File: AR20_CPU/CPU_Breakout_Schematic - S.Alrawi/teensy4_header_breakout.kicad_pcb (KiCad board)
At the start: 4 copper layers, 11 parts, among them J1 Conn_2Rows-34Pins, J3 Micro_SD_Card, SW1 SW_SPST, U1 Teensy_pins, U2 MCP2551-I-SN

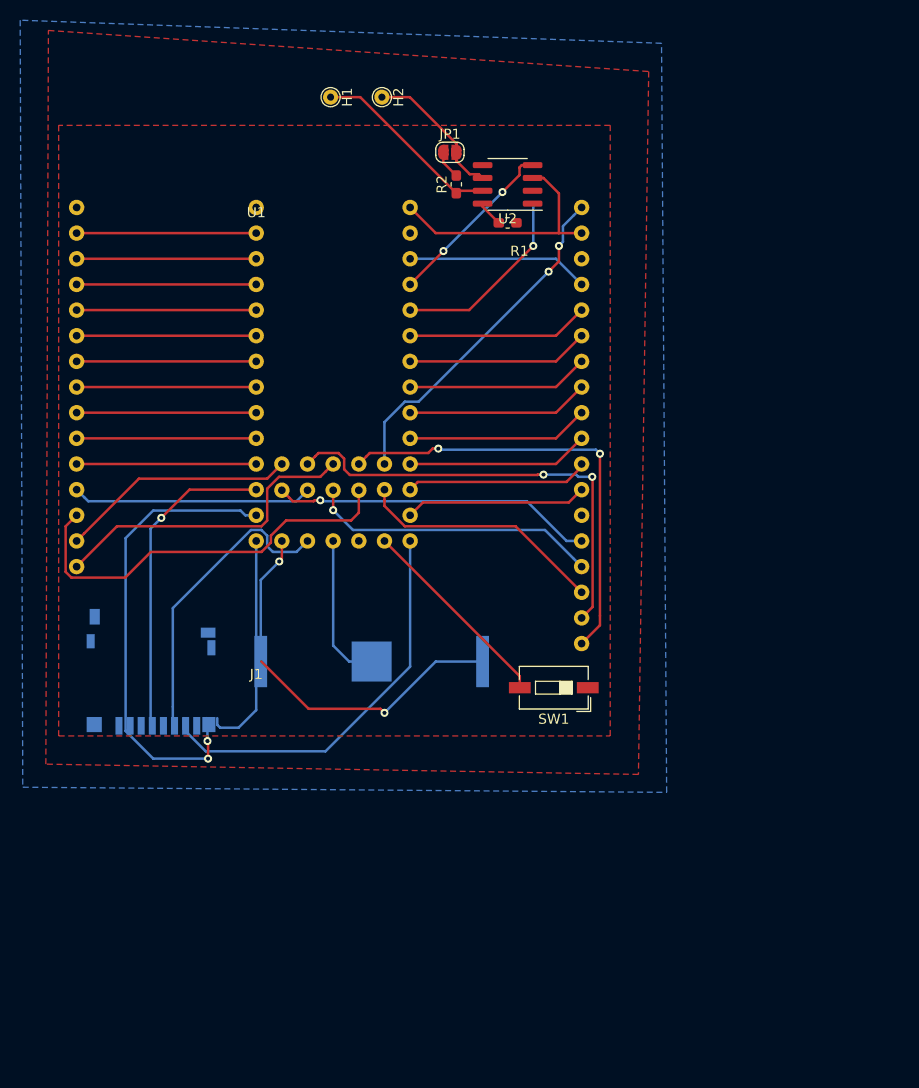
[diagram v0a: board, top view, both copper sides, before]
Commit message: Edited library
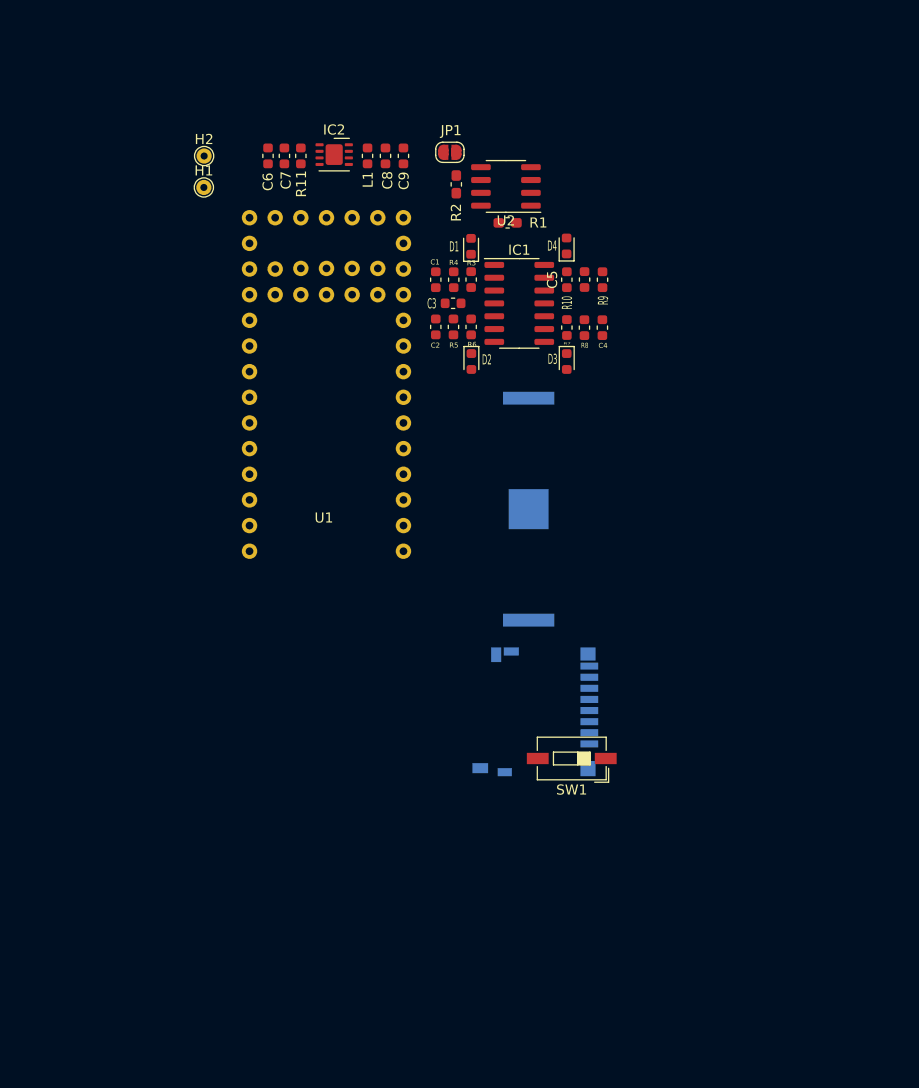
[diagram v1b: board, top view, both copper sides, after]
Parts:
- removed J1: Conn_2Rows-34Pins, Teensy_Footprint_Library:PINS_IO_TEENSY
- added C1: 1.5n, Capacitor_SMD:C_0603_1608Metric, F.Cu at (142.7, 79.3)
- added C2: 1.5n, Capacitor_SMD:C_0603_1608Metric, F.Cu at (142.7, 84.0)
- added C3: C, Capacitor_SMD:C_0603_1608Metric, F.Cu at (144.5, 81.6)
- added C4: 1.5n, Capacitor_SMD:C_0603_1608Metric, F.Cu at (159.2, 84.0)
- added C5: 1.5n, Capacitor_SMD:C_0603_1608Metric, F.Cu at (155.7, 79.3)
- added C6: 10u, Capacitor_SMD:C_0603_1608Metric, F.Cu at (126.1, 67.0)
- added C7: 0.1u, Capacitor_SMD:C_0603_1608Metric, F.Cu at (127.8, 67.0)
- added C8: 0.1u, Capacitor_SMD:C_0603_1608Metric, F.Cu at (137.8, 67.0)
- added C9: 10u, Capacitor_SMD:C_0603_1608Metric, F.Cu at (139.5, 67.0)
- added D1: 3V, Diode_SMD:D_0603_1608Metric, F.Cu at (146.2, 76.0)
- added D2: 3V, Diode_SMD:D_0603_1608Metric, F.Cu at (146.3, 87.4)
- added D3: 3V, Diode_SMD:D_0603_1608Metric, F.Cu at (155.7, 87.4)
- added D4: 3V, Diode_SMD:D_0603_1608Metric, F.Cu at (155.7, 75.9)
- added IC1: LM324DRG3, Package_SO:SOIC-14_3.9x8.7mm_P1.27mm, F.Cu at (151.0, 81.6)
- added IC2: NCV890430MW50TXG, Package_DFN_QFN:DFN-8-1EP_3x3mm_P0.65mm_EP1.7x2.05mm, F.Cu at (132.7, 66.9)
- added L1: 2.2u, Inductor_SMD:L_0603_1608Metric, F.Cu at (136.0, 67.0)
- added R10: 20k, Resistor_SMD:R_0603_1608Metric, F.Cu at (157.5, 79.3)
- added R11: 10k, Resistor_SMD:R_0603_1608Metric, F.Cu at (129.4, 67.0)
- added R3: 10k, Resistor_SMD:R_0603_1608Metric, F.Cu at (146.2, 79.3)
- added R4: 20k, Resistor_SMD:R_0603_1608Metric, F.Cu at (144.5, 79.3)
- added R5: 10k, Resistor_SMD:R_0603_1608Metric, F.Cu at (146.2, 84.0)
- added R6: 20k, Resistor_SMD:R_0603_1608Metric, F.Cu at (144.5, 84.0)
- added R7: 10k, Resistor_SMD:R_0603_1608Metric, F.Cu at (155.7, 84.0)
- added R8: 20k, Resistor_SMD:R_0603_1608Metric, F.Cu at (157.5, 84.0)
- added R9: 10k, Resistor_SMD:R_0603_1608Metric, F.Cu at (159.3, 79.3)
- moved J3 38.3 mm to (152.6, 122.1), turned to 270 degrees
- moved U1 37.0 mm to (139.5, 106.2), turned to 180 degrees
- moved BT1 21.7 mm to (151.9, 102.0), turned to 270 degrees
- moved H2 18.5 mm to (119.8, 67.0), turned to 0 degrees
- moved H1 15.4 mm to (119.8, 70.2), turned to 0 degrees
- moved SW1 7.23 mm to (156.2, 126.7)
- moved U2 0.26 mm to (149.7, 70.1)
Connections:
- J3 pad 2: 10_CS -> (no net)
- J3 pad 3: (no net) -> 10_CS
- U1 pad 12: 21_A7 -> Out1
- U1 pad 14: 20_A6 -> Out2
- U1 pad 16: 19_A5 -> Out3
- U1 pad 18: 18_A4 -> Out4
- U1 pad 32: PROGRAMM -> (no net)
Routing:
- net 11_MOSI: track 46.7 -> 0.00 mm, vias 2 -> 0
- net 30_CRX3: track 44.7 -> 0.00 mm, vias 2 -> 0
- net 32_OUT1B: track 44.3 -> 0.00 mm, vias 2 -> 0
- net 27_A13: track 40.6 -> 0.00 mm
- net 13(LED): track 40.3 -> 0.00 mm
- net VBAT: track 38.9 -> 0.00 mm, vias 2 -> 0
- net 33_MCLK2: track 34.3 -> 0.00 mm, vias 2 -> 0
- net 24_A10: track 31.8 -> 0.00 mm, vias 1 -> 0
- net 31_CTX3: track 31.5 -> 0.00 mm
- net 10_CS: track 30.8 -> 0.00 mm, vias 1 -> 0
- net 3V3: track 29.4 -> 0.00 mm
- net 26_A12: track 28.9 -> 0.00 mm, vias 1 -> 0
- net Vinn_5V: track 25.2 -> 0.00 mm
- net 28_RX7: track 24.7 -> 0.00 mm
- net 25_A11: track 23.8 -> 0.00 mm
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- removed copper zone on B.Cu, net Ground
- removed copper zone on F.Cu, net Ground
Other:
- copper layers 4 -> 2
- rule pad_to_mask_clearance: 0 -> 0.0508
- rule trace_min: 0.007 -> 0.25

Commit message: Edited the layout
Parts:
- removed J3: Micro_SD_Card, Connector_Card:microSD_HC_Hirose_DM3D-SF
- removed U1: Teensy_pins, Teensy_Footprint_Library:Teensy_40_footprint
- removed U2: MCP2551-I-SN, Package_SO:SOIC-8_3.9x4.9mm_P1.27mm
- added C10: 1.5n, Capacitor_SMD:C_0603_1608Metric, F.Cu at (158.2, 81.4)
- added CANmodule1: MCP2551-I-SN, Package_SO:SOIC-8_3.9x4.9mm_P1.27mm, F.Cu at (138.5, 82.9)
- added GND1: GND, TestPoint:TestPoint_THTPad_D1.5mm_Drill0.7mm, F.Cu at (116.7, 117.3)
- added J1: MX34_36_pins, Teensy_Footprint_Library:Connector_MX34_36pins, F.Cu at (131.2, 124.8)
- added JP2: SJ_Open, Jumper:SolderJumper-2_P1.3mm_Open_RoundedPad1.0x1.5mm, B.Cu at (143.3, 80.0)
- added JP3: SJ_Open, Jumper:SolderJumper-2_P1.3mm_Open_RoundedPad1.0x1.5mm, B.Cu at (143.5, 86.2)
- added JP4: SJ_Open, Jumper:SolderJumper-2_P1.3mm_Open_RoundedPad1.0x1.5mm, F.Cu at (159.2, 89.0)
- added JP5: SJ_Open, Jumper:SolderJumper-2_P1.3mm_Open_RoundedPad1.0x1.5mm, F.Cu at (158.5, 78.2)
- added MX34_Housing1: MX34_Housing, Teensy_Footprint_Library:Housing_3pins, F.Cu at (116.7, 130.6)
- added R12: 20k, Resistor_SMD:R_0603_1608Metric, F.Cu at (156.3, 81.4)
- added SDcard1: Micro_SD_Card, Connector_Card:microSD_HC_Hirose_DM3D-SF, F.Cu at (119.8, 83.0)
- added Teensy4.0: Teensy_pins, Teensy_Footprint_Library:Teensy_40_footprint, F.Cu at (123.3, 107.7)
- C2: value 1.5n -> 10u
- R6: value 20k -> 10k
- moved SW1 47.7 mm to (116.1, 101.0), turned to 270 degrees
- moved H2 45.3 mm to (116.7, 112.2)
- moved H1 44.7 mm to (116.8, 114.8)
- moved R6 27.7 mm to (117.7, 90.7), turned to 180 degrees
- moved C9 24.0 mm to (130.7, 89.3), turned to 0 degrees
- moved BT1 22.0 mm to (141.4, 121.3), turned to 180 degrees
- moved C8 21.7 mm to (130.7, 87.5), turned to 0 degrees
- moved L1 19.4 mm to (130.7, 85.7), turned to 180 degrees
- moved R1 16.6 mm to (134.8, 80.8), turned to 90 degrees
- moved C4 15.9 mm to (143.5, 86.1)
- moved SWReg_NVC1 15.6 mm to (130.8, 82.4), turned to 270 degrees
- moved R8 12.5 mm to (145.2, 86.1)
- moved R11 12.2 mm to (130.7, 79.1), turned to 180 degrees
- moved JP1 10.9 mm to (141.9, 77.3), turned to 270 degrees
- moved C7 10.9 mm to (130.7, 77.5), turned to 180 degrees
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- renumbered IC1 to LM324, IC2 to SWReg_NVC1
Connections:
- BT1 pad 2: GND_BATT -> Ground
- C1 pad 2: Ground -> Net-(C1-Pad2)
- C2 pad 1: IN2+ -> Vinn_5V
- C2 pad 2: Ground -> Net-(C2-Pad2)
- C4 pad 1: IN3+ -> IN2+
- C4 pad 2: Ground -> Net-(C4-Pad2)
- C5 pad 1: IN4+ -> IN3+
- C5 pad 2: Ground -> Net-(C5-Pad2)
- LM324 pad 11: (no net) -> Ground
- R10 pad 1: IN4+ -> IN3+
- R3 pad 1: (no net) -> Sensor_Input_1
- R5 pad 1: (no net) -> Sensor_Input_2
- R6 pad 1: IN2+ -> 3.3V
- R6 pad 2: Ground -> 13(LED)
- R7 pad 1: (no net) -> Sensor_Input_3
- R8 pad 1: IN3+ -> IN2+
- R9 pad 1: (no net) -> Sensor_Input_4
- SWReg_NVC1 pad 9: Ground -> (no net)
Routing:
- net 12V_IN: track 0.00 -> 78.1 mm, vias 0 -> 4
- net 13(LED): track 0.00 -> 66.4 mm, vias 0 -> 2
- net 11_MOSI: track 0.00 -> 62.9 mm, vias 0 -> 4
- net Net-(CANmodule1-Pad6): track 0.00 -> 62.5 mm, vias 0 -> 3
- net 12_MISO: track 0.00 -> 58.5 mm, vias 0 -> 5
- net 10_CS: track 0.00 -> 57.5 mm, vias 0 -> 1
- net Net-(CANmodule1-Pad7): track 0.00 -> 55.0 mm, vias 0 -> 3
- net ON_OFF: track 0.00 -> 52.0 mm, vias 0 -> 1
- net Vinn_5V: track 0.00 -> 50.3 mm, vias 0 -> 4
- net VBAT: track 0.00 -> 45.8 mm
- net Sensor_Input_1: track 0.00 -> 39.6 mm, vias 0 -> 2
- net 15_A1: track 0.00 -> 38.3 mm
- net 16_A2: track 0.00 -> 38.1 mm
- net 17_A3: track 0.00 -> 37.9 mm
- net Sensor_Input_4: track 0.00 -> 36.7 mm
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- added copper zone on B.Cu, net Ground
- added copper zone on F.Cu, net Ground
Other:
- board outline added: 57 x 60 mm
- board text added: "AR20 Teensy 4.0"

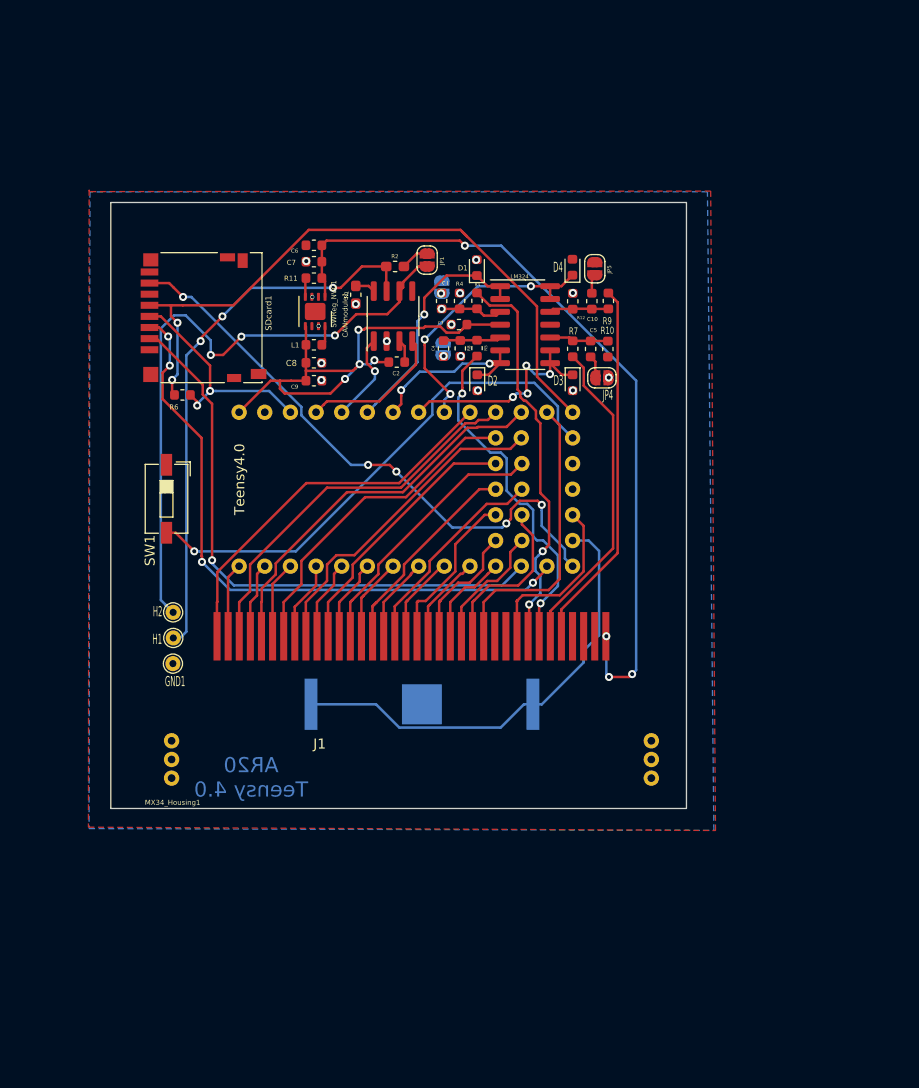
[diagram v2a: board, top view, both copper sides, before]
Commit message: Edited to 4 layers
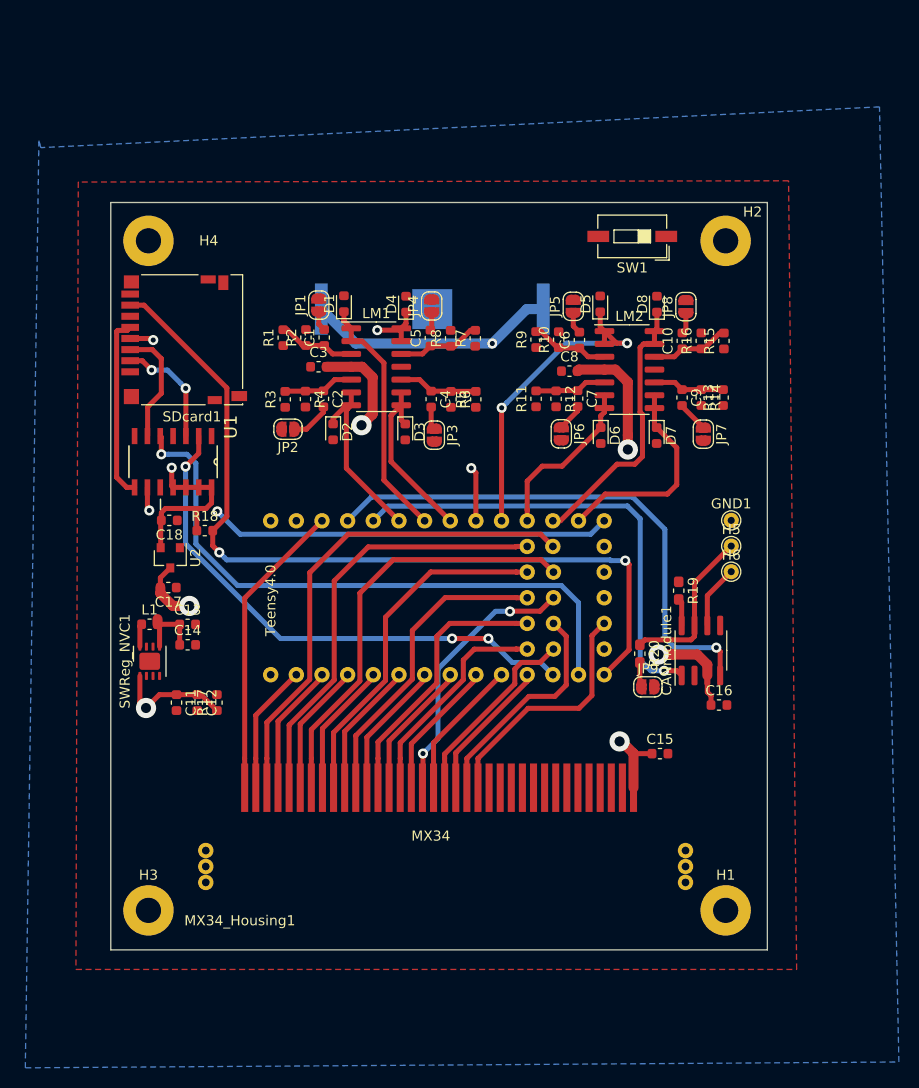
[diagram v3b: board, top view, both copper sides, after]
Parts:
- removed J1: MX34_36_pins, Teensy_Footprint_Library:Connector_MX34_36pins
- removed LM324: LM324DRG3, Package_SO:SOIC-14_3.9x8.7mm_P1.27mm
- added C11: 10u, Capacitor_SMD:C_0603_1608Metric, F.Cu at (117.1, 121.2)
- added C12: 0.1u, Capacitor_SMD:C_0603_1608Metric, F.Cu at (119.1, 121.2)
- added C13: 0.1u, Capacitor_SMD:C_0603_1608Metric, F.Cu at (118.2, 113.4)
- added C14: 10u, Capacitor_SMD:C_0603_1608Metric, F.Cu at (118.2, 115.4)
- added C15: 10u, Capacitor_SMD:C_0603_1608Metric, F.Cu at (164.9, 126.2)
- added C16: 100u, Capacitor_SMD:C_0603_1608Metric, F.Cu at (170.8, 121.4)
- added C17: 100u, Capacitor_SMD:C_0603_1608Metric, F.Cu at (116.3, 109.8)
- added C18: 100u, Capacitor_SMD:C_0603_1608Metric, F.Cu at (116.4, 103.1)
- added D5: 3V, Diode_SMD:D_0603_1608Metric, F.Cu at (159.0, 81.7)
- added D6: 3V, Diode_SMD:D_0603_1608Metric, F.Cu at (159.1, 94.7)
- added D7: 3V, Diode_SMD:D_0603_1608Metric, F.Cu at (164.6, 94.7)
- added D8: 3V, Diode_SMD:D_0603_1608Metric, F.Cu at (164.6, 81.7)
- added H3: MountingHole, MountingHole:MountingHole_2.5mm_Pad, F.Cu at (114.3, 141.7)
- added H4: MountingHole, MountingHole:MountingHole_2.5mm_Pad, F.Cu at (114.3, 75.4)
- added H5: CANH_out, TestPoint:TestPoint_THTPad_D1.5mm_Drill0.7mm, F.Cu at (172.0, 105.7)
- added H6: CANL_out, TestPoint:TestPoint_THTPad_D1.5mm_Drill0.7mm, F.Cu at (172.0, 108.2)
- added JP6: SJ_Open, Jumper:SolderJumper-2_P1.3mm_Open_RoundedPad1.0x1.5mm, F.Cu at (155.2, 94.5)
- added JP7: SJ_Open, Jumper:SolderJumper-2_P1.3mm_Open_RoundedPad1.0x1.5mm, F.Cu at (169.2, 94.6)
- added JP8: SJ_Open, Jumper:SolderJumper-2_P1.3mm_Open_RoundedPad1.0x1.5mm, F.Cu at (167.5, 82.0)
- added JP9: SolderJumper_2_Open, Jumper:SolderJumper-2_P1.3mm_Open_RoundedPad1.0x1.5mm, F.Cu at (163.8, 119.6)
- added LM1: LM324DRG3, Package_SO:SOIC-14_3.9x8.7mm_P1.27mm, F.Cu at (136.9, 87.9)
- added LM2: LM324DRG3, Package_SO:SOIC-14_3.9x8.7mm_P1.27mm, F.Cu at (161.9, 88.2)
- added MX34: MX34_36_pins, Teensy_Footprint_Library:Connector_MX34_36pins, F.Cu at (134.0, 139.7)
- added R13: 10k, Resistor_SMD:R_0603_1608Metric, F.Cu at (171.2, 91.0)
- added R14: 20k, Resistor_SMD:R_0603_1608Metric, F.Cu at (169.0, 91.0)
- added R15: 10k, Resistor_SMD:R_0603_1608Metric, F.Cu at (171.3, 85.4)
- added R16: 20k, Resistor_SMD:R_0603_1608Metric, F.Cu at (169.0, 85.3)
- added R17: 10k, Resistor_SMD:R_0603_1608Metric, F.Cu at (121.1, 121.2)
- added R18: 10k, Resistor_SMD:R_0603_1608Metric, F.Cu at (119.9, 104.1)
- added R19: 60, Resistor_SMD:R_0603_1608Metric_Pad1.05x0.95mm_HandSolder, F.Cu at (166.8, 110.1)
- added R20: 120, Resistor_SMD:R_0603_1608Metric_Pad1.05x0.95mm_HandSolder, F.Cu at (163.0, 116.3)
- added U1: 74LCX125M, SamacSys_Parts:SOIC127P600X175-14N, F.Cu at (116.7, 97.3)
- added U2: MCP1700_SOT23, Package_TO_SOT_SMD:SOT-23, F.Cu at (116.5, 106.8)
- C2, C6, C9: value 10u -> 1.5n
- C7: value 0.1u -> 1.5n
- C8: value 0.1u -> C
- H1: value CANH_out -> GND; footprint TestPoint:TestPoint_THTPad_D1.5mm_Drill0.7mm -> MountingHole:MountingHole_2.5mm_Pad
- H2: value CANL_out -> MountingHole; footprint TestPoint:TestPoint_THTPad_D1.5mm_Drill0.7mm -> MountingHole:MountingHole_2.5mm_Pad
- JP1: value SolderJumper_2_Open -> SJ_Open
- JP2, JP3: moved to F.Cu
- R1: value 60 -> 10k; footprint Resistor_SMD:R_0603_1608Metric_Pad1.05x0.95mm_HandSolder -> Resistor_SMD:R_0603_1608Metric
- R2: value 120 -> 20k; footprint Resistor_SMD:R_0603_1608Metric_Pad1.05x0.95mm_HandSolder -> Resistor_SMD:R_0603_1608Metric
- R6: value 10k -> 20k
- moved H2 65.9 mm to (171.4, 75.4)
- moved H1 61.0 mm to (171.4, 141.7)
- moved GND1 57.1 mm to (172.0, 103.1)
- moved SW1 52.9 mm to (162.2, 75.0), turned to 180 degrees
- moved CANmodule1 45.0 mm to (169.0, 116.0)
- moved BT1 39.1 mm to (142.4, 82.2), turned to 0 degrees
- moved SWReg_NVC1 38.3 mm to (114.4, 117.1), turned to 90 degrees
- moved C9 36.5 mm to (167.1, 91.0), turned to 270 degrees
- moved L1 32.1 mm to (114.4, 113.4), turned to 0 degrees
- moved C7 29.4 mm to (156.8, 91.1), turned to 270 degrees
- moved C6 27.9 mm to (157.0, 85.3), turned to 90 degrees
- moved R6 26.6 mm to (144.2, 91.1), turned to 270 degrees
- moved C8 25.3 mm to (156.0, 88.3)
- moved R11 25.0 mm to (152.7, 91.1), turned to 90 degrees
- moved R3 21.3 mm to (127.8, 91.1), turned to 90 degrees
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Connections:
- C10 pad 1: IN4+ -> IN8+
- C2 pad 1: Vinn_5V -> IN2+
- C4 pad 1: IN2+ -> IN3+
- C5 pad 1: IN3+ -> IN4+
- C6 pad 1: 12V_IN -> IN5+
- C6 pad 2: Ground -> Net-(C6-Pad2)
- C7 pad 1: 12V_IN -> IN6+
- C7 pad 2: Ground -> Net-(C7-Pad2)
- C8 pad 1: Vinn_5V -> Ground
- C8 pad 2: Ground -> Vinn_5V
- C9 pad 1: Vinn_5V -> IN7+
- C9 pad 2: Ground -> Net-(C9-Pad2)
- CANmodule1 pad 3: Net-(C2-Pad2) -> Vinn_5V
- H1 pad 1: Net-(CANmodule1-Pad7) -> (no net)
- H2 pad 1: Net-(CANmodule1-Pad6) -> (no net)
- JP1 pad 1: Net-(JP1-Pad1) -> Net-(C1-Pad2)
- JP1 pad 2: Net-(CANmodule1-Pad6) -> Ground
- JP2 pad 1: Net-(C1-Pad2) -> Net-(C2-Pad2)
- JP5 pad 1: Net-(C10-Pad2) -> Net-(C6-Pad2)
- R1 pad 1: Ground -> Sensor_Input_1
- R1 pad 2: Net-(CANmodule1-Pad8) -> IN1+
- R10 pad 1: IN3+ -> IN5+
- R11 pad 1: 12V_IN -> Sensor_Input_6
- R11 pad 2: Net-(R11-Pad2) -> IN6+
- R12 pad 1: IN4+ -> IN6+
- R2 pad 1: Net-(CANmodule1-Pad7) -> IN1+
- R2 pad 2: Net-(JP1-Pad1) -> Ground
- R3 pad 1: Sensor_Input_1 -> Sensor_Input_2
- R3 pad 2: IN1+ -> IN2+
- R4 pad 1: IN1+ -> IN2+
- R5 pad 1: Sensor_Input_2 -> Sensor_Input_3
- R5 pad 2: IN2+ -> IN3+
- R6 pad 1: 3.3V -> IN3+
- R6 pad 2: 13(LED) -> Ground
- R7 pad 1: Sensor_Input_3 -> Sensor_Input_4
- R7 pad 2: IN3+ -> IN4+
- R8 pad 1: IN2+ -> IN4+
- R9 pad 1: Sensor_Input_4 -> Sensor_Input_5
- R9 pad 2: IN4+ -> IN5+
- SDcard1 pad 2: 10_CS -> CS_3.3V
- SDcard1 pad 3: 11_MOSI -> MOSI_3.3V
- SDcard1 pad 4: 3.3V -> 3V3_SD
- SDcard1 pad 5: 13(LED) -> SCLK_3.3V
- SWReg_NVC1 pad 4: Net-(R11-Pad2) -> Net-(R17-Pad2)
- SWReg_NVC1 pad 9: (no net) -> Ground
- Teensy4.0 pad 12: Out1 -> Out2
- Teensy4.0 pad 14: Out2 -> Out1
- Teensy4.0 pad 20: 17_A3 -> Out5
- Teensy4.0 pad 22: 16_A2 -> Out6
- Teensy4.0 pad 24: 15_A1 -> Out8
- Teensy4.0 pad 26: 14_A0 -> Out7
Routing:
- net Vinn_5V: track 50.3 -> 145.5 mm
- net Net-(CANmodule1-Pad6): track 62.5 -> 6.30 mm, vias 3 -> 0
- net ON_OFF: track 52.0 -> 0.00 mm, vias 1 -> 0
- net Sensor_Input_1: track 39.6 -> 0.00 mm, vias 2 -> 0
- net Net-(CANmodule1-Pad7): track 55.0 -> 16.2 mm, vias 3 -> 0
- net 23_CRX1: track 14.3 -> 52.9 mm, vias 0 -> 1
- net 15_A1: track 38.3 -> 0.00 mm
- net 16_A2: track 38.1 -> 0.00 mm
- net 17_A3: track 37.9 -> 0.00 mm
- net 22_CTX1: track 9.02 -> 46.3 mm
- net Sensor_Input_4: track 36.7 -> 0.00 mm
- net Sensor_Input_2: track 34.7 -> 0.00 mm, vias 2 -> 0
- net 3V3_SD: track 0.00 -> 34.2 mm, vias 0 -> 2
- net Out5: track 0.00 -> 32.4 mm, vias 0 -> 2
- net Sensor_Input_3: track 31.9 -> 0.00 mm
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- added copper zone on Back_2_3V3, net 3V3_SD
- added copper zone on Front_2_5V, net Vinn_5V
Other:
- board size 57 x 60 mm -> 65 x 74 mm
- copper layers 2 -> 4
- board text removed: "AR20 Teensy 4.0"
